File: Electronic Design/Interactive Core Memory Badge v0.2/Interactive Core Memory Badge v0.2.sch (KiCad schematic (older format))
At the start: 59 parts, among them Q1 MMBT4403LT1G, Q10 MMBT4401LT1G, Q11 MMBT4403LT1G, Q12 MMBT4401LT1G, Q13 MMBT4403LT1G, Q14 MMBT4401LT1G, Q15 MMBT4403LT1G, Q16 MMBT4401LT1G, Q17 MMBT4403LT1G, Q18 MMBT4401LT1G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

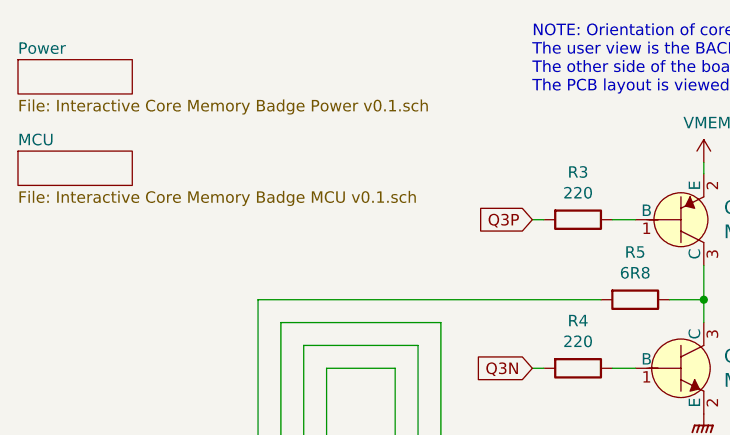
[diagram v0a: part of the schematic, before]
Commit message: Adding discrete OR gate
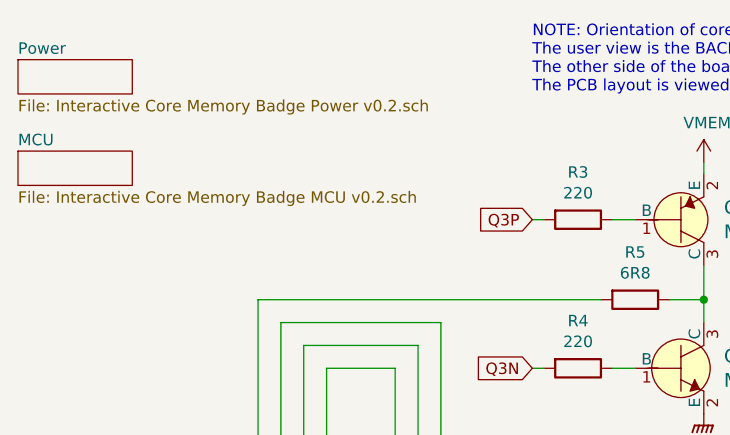
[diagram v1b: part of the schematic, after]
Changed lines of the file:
@@
 EESchema Schematic File Version 4
+LIBS:Interactive Core Memory Badge v0.2-cache
 EELAYER 29 0
 EELAYER END
@@
 U 5D254AE8
 F0 "Power" 50
-F1 "Interactive Core Memory Badge Power v0.1.sch" 50
+F1 "Interactive Core Memory Badge Power v0.2.sch" 50
 $EndSheet
 $Sheet
@@
 U 5D2551FF
 F0 "MCU" 50
-F1 "Interactive Core Memory Badge MCU v0.1.sch" 50
+F1 "Interactive Core Memory Badge MCU v0.2.sch" 50
 $EndSheet
 Text GLabel 1750 4600 3    50   Input ~ 0

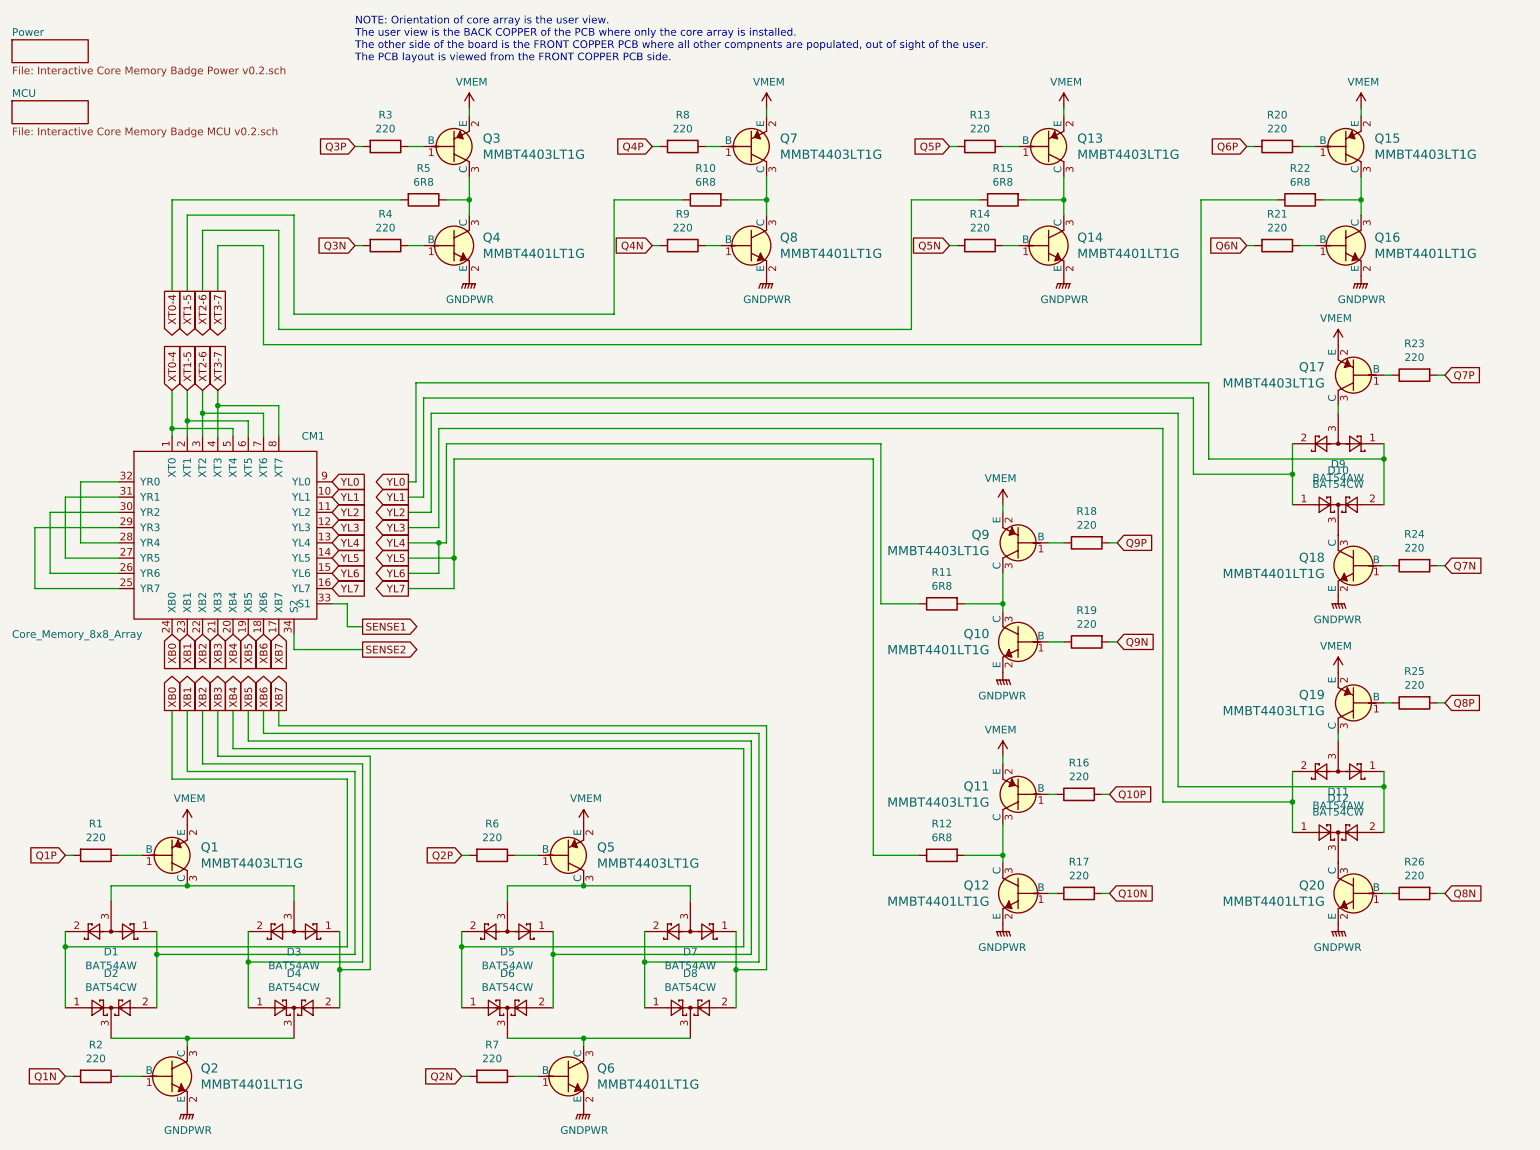
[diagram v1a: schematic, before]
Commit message: Updated drive transistors, switch/diode, OR gate, layout
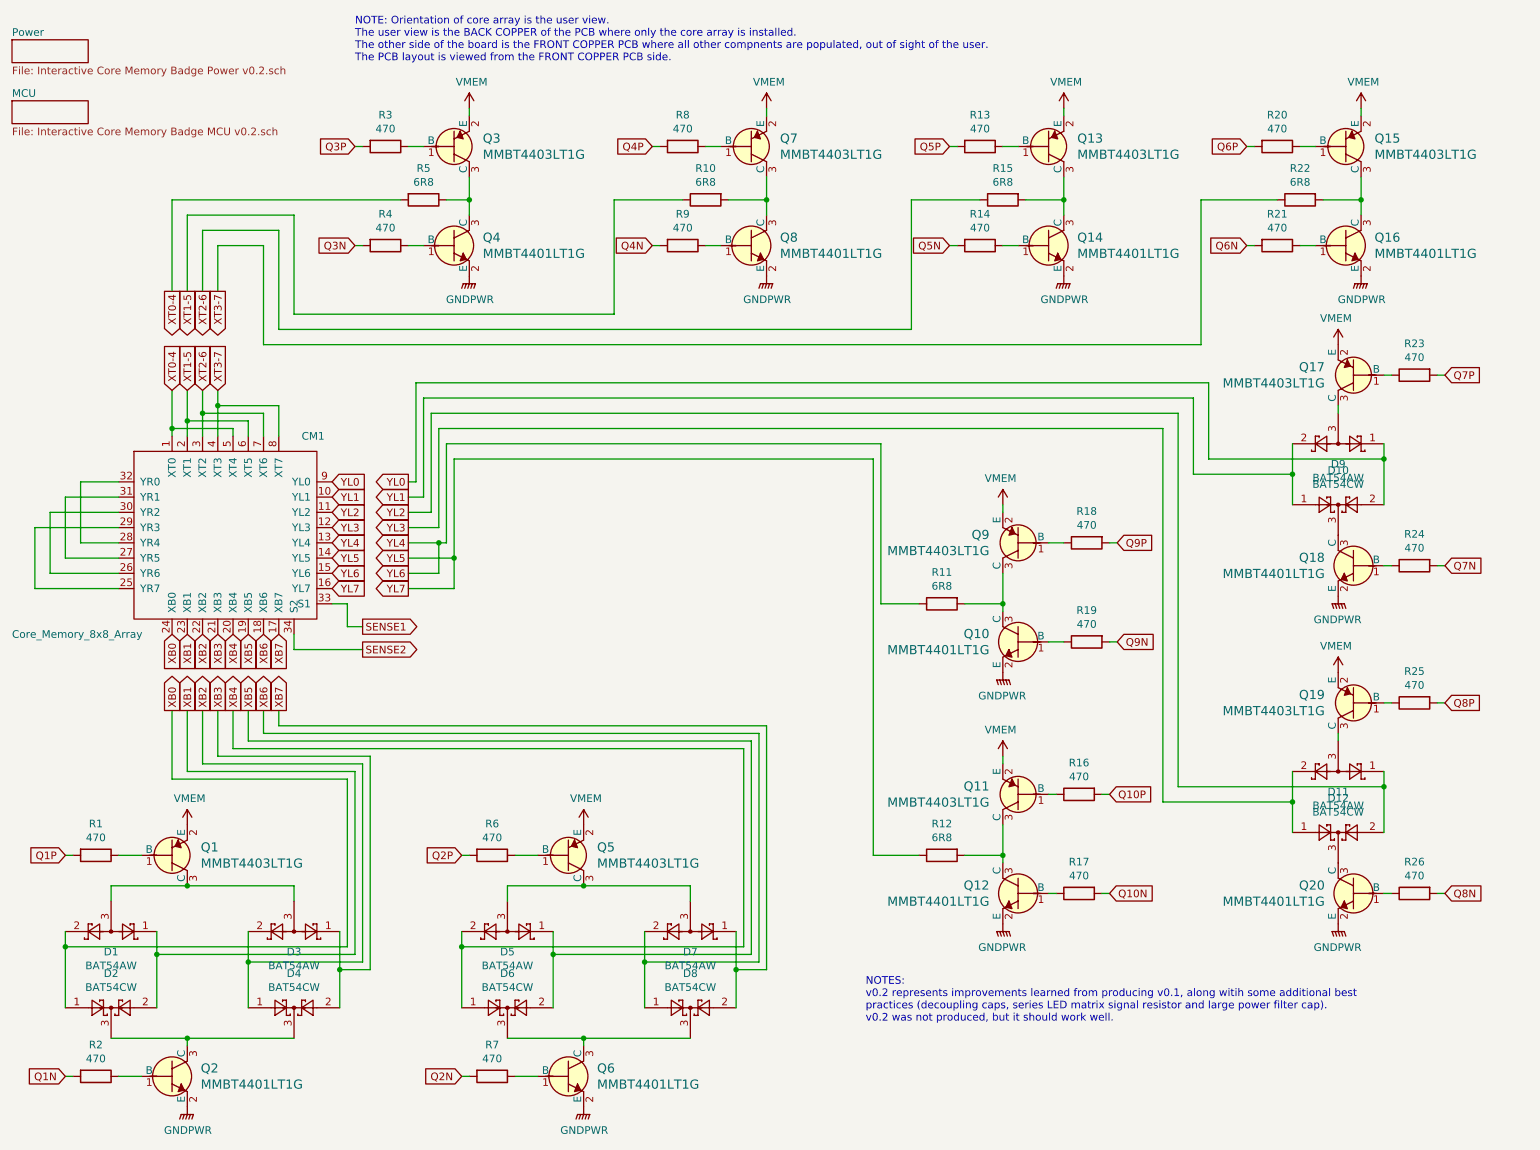
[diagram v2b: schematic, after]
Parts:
- R1, R13, R14, R16, R17, R18, R19, R2, R20, R21, R23, R24, R25, R26, R3, R4, R6, R7, R8, R9: value 220 -> 470
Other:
- note added: "NOTES:\nv0.2 represents improvements learned from producing v0.1, along witih some additional best\npractices (decoupling caps, series LED matrix signal resistor and large power filter cap).\nv0.2 was not produced, but it should work well."
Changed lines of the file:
@@
 encoding utf-8
 Sheet 1 3
-Title "Core 64"
-Date "2019-07-09"
-Rev "0.1"
-Comp "Andy Geppert"
+Title "Core 64 - Interactive Core Memory Badge"
+Date "2020-03-05"
+Rev "0.2"
+Comp "Andy Geppert - Machine Ideas, LLC"
 Comment1 ""
 Comment2 ""
@@
 P 3150 1400
 F 0 "R3" V 2943 1400 50  0000 C CNN
-F 1 "220" V 3034 1400 50  0000 C CNN
+F 1 "470" V 3034 1400 50  0000 C CNN
 F 2 "Resistor_SMD:R_0805_2012Metric" V 3080 1400 50  0001 C CNN
 F 3 "~" H 3150 1400 50  0001 C CNN
@@
 P 3150 2050
 F 0 "R4" V 2943 2050 50  0000 C CNN
-F 1 "220" V 3034 2050 50  0000 C CNN
+F 1 "470" V 3034 2050 50  0000 C CNN
 F 2 "Resistor_SMD:R_0805_2012Metric" V 3080 2050 50  0001 C CNN
 F 3 "~" H 3150 2050 50  0001 C CNN
@@
 P 3850 6050
 F 0 "R6" V 3643 6050 50  0000 C CNN
-F 1 "220" V 3734 6050 50  0000 C CNN
+F 1 "470" V 3734 6050 50  0000 C CNN
 F 2 "Resistor_SMD:R_0805_2012Metric" V 3780 6050 50  0001 C CNN
 F 3 "~" H 3850 6050 50  0001 C CNN
@@
 P 3850 7500
 F 0 "R7" V 3643 7500 50  0000 C CNN
-F 1 "220" V 3734 7500 50  0000 C CNN
+F 1 "470" V 3734 7500 50  0000 C CNN
 F 2 "Resistor_SMD:R_0805_2012Metric" V 3780 7500 50  0001 C CNN
 F 3 "~" H 3850 7500 50  0001 C CNN
@@
 P 5100 1400
 F 0 "R8" V 4893 1400 50  0000 C CNN
-F 1 "220" V 4984 1400 50  0000 C CNN
+F 1 "470" V 4984 1400 50  0000 C CNN
 F 2 "Resistor_SMD:R_0805_2012Metric" V 5030 1400 50  0001 C CNN
 F 3 "~" H 5100 1400 50  0001 C CNN
@@
 P 5100 2050
 F 0 "R9" V 4893 2050 50  0000 C CNN
-F 1 "220" V 4984 2050 50  0000 C CNN
+F 1 "470" V 4984 2050 50  0000 C CNN
 F 2 "Resistor_SMD:R_0805_2012Metric" V 5030 2050 50  0001 C CNN
 F 3 "~" H 5100 2050 50  0001 C CNN
@@
 P 7050 1400
 F 0 "R13" V 6843 1400 50  0000 C CNN
-F 1 "220" V 6934 1400 50  0000 C CNN
+F 1 "470" V 6934 1400 50  0000 C CNN
 F 2 "Resistor_SMD:R_0805_2012Metric" V 6980 1400 50  0001 C CNN
 F 3 "~" H 7050 1400 50  0001 C CNN
@@
 P 7050 2050
 F 0 "R14" V 6843 2050 50  0000 C CNN
-F 1 "220" V 6934 2050 50  0000 C CNN
+F 1 "470" V 6934 2050 50  0000 C CNN
 F 2 "Resistor_SMD:R_0805_2012Metric" V 6980 2050 50  0001 C CNN
 F 3 "~" H 7050 2050 50  0001 C CNN
@@
 P 9000 1400
 F 0 "R20" V 8793 1400 50  0000 C CNN
-F 1 "220" V 8884 1400 50  0000 C CNN
+F 1 "470" V 8884 1400 50  0000 C CNN
 F 2 "Resistor_SMD:R_0805_2012Metric" V 8930 1400 50  0001 C CNN
 F 3 "~" H 9000 1400 50  0001 C CNN
@@
 P 9000 2050
 F 0 "R21" V 8793 2050 50  0000 C CNN
-F 1 "220" V 8884 2050 50  0000 C CNN
+F 1 "470" V 8884 2050 50  0000 C CNN
 F 2 "Resistor_SMD:R_0805_2012Metric" V 8930 2050 50  0001 C CNN
 F 3 "~" H 9000 2050 50  0001 C CNN
@@
 P 9900 2900
 F 0 "R23" V 9693 2900 50  0000 C CNN
-F 1 "220" V 9784 2900 50  0000 C CNN
+F 1 "470" V 9784 2900 50  0000 C CNN
 F 2 "Resistor_SMD:R_0805_2012Metric" V 9830 2900 50  0001 C CNN
 F 3 "~" H 9900 2900 50  0001 C CNN
@@
 P 9900 4150
 F 0 "R24" V 9693 4150 50  0000 C CNN
-F 1 "220" V 9784 4150 50  0000 C CNN
+F 1 "470" V 9784 4150 50  0000 C CNN
 F 2 "Resistor_SMD:R_0805_2012Metric" V 9830 4150 50  0001 C CNN
 F 3 "~" H 9900 4150 50  0001 C CNN
@@
 P 9900 5050
 F 0 "R25" V 9693 5050 50  0000 C CNN
-F 1 "220" V 9784 5050 50  0000 C CNN
+F 1 "470" V 9784 5050 50  0000 C CNN
 F 2 "Resistor_SMD:R_0805_2012Metric" V 9830 5050 50  0001 C CNN
 F 3 "~" H 9900 5050 50  0001 C CNN
@@
 P 9900 6300
 F 0 "R26" V 9693 6300 50  0000 C CNN
-F 1 "220" V 9784 6300 50  0000 C CNN
+F 1 "470" V 9784 6300 50  0000 C CNN
 F 2 "Resistor_SMD:R_0805_2012Metric" V 9830 6300 50  0001 C CNN
 F 3 "~" H 9900 6300 50  0001 C CNN
@@
 P 7750 4000
 F 0 "R18" V 7543 4000 50  0000 C CNN
-F 1 "220" V 7634 4000 50  0000 C CNN
+F 1 "470" V 7634 4000 50  0000 C CNN
 F 2 "Resistor_SMD:R_0805_2012Metric" V 7680 4000 50  0001 C CNN
 F 3 "~" H 7750 4000 50  0001 C CNN
@@
 P 7750 4650
 F 0 "R19" V 7543 4650 50  0000 C CNN
-F 1 "220" V 7634 4650 50  0000 C CNN
+F 1 "470" V 7634 4650 50  0000 C CNN
 F 2 "Resistor_SMD:R_0805_2012Metric" V 7680 4650 50  0001 C CNN
 F 3 "~" H 7750 4650 50  0001 C CNN
@@
 P 7700 5650
 F 0 "R16" V 7493 5650 50  0000 C CNN
-F 1 "220" V 7584 5650 50  0000 C CNN
+F 1 "470" V 7584 5650 50  0000 C CNN
 F 2 "Resistor_SMD:R_0805_2012Metric" V 7630 5650 50  0001 C CNN
 F 3 "~" H 7700 5650 50  0001 C CNN
@@
 P 7700 6300
 F 0 "R17" V 7493 6300 50  0000 C CNN
-F 1 "220" V 7584 6300 50  0000 C CNN
+F 1 "470" V 7584 6300 50  0000 C CNN
 F 2 "Resistor_SMD:R_0805_2012Metric" V 7630 6300 50  0001 C CNN
 F 3 "~" H 7700 6300 50  0001 C CNN
@@
 P 1250 6050
 F 0 "R1" V 1043 6050 50  0000 C CNN
-F 1 "220" V 1134 6050 50  0000 C CNN
+F 1 "470" V 1134 6050 50  0000 C CNN
 F 2 "Resistor_SMD:R_0805_2012Metric" V 1180 6050 50  0001 C CNN
 F 3 "~" H 1250 6050 50  0001 C CNN
@@
 P 1250 7500
 F 0 "R2" V 1043 7500 50  0000 C CNN
-F 1 "220" V 1134 7500 50  0000 C CNN
+F 1 "470" V 1134 7500 50  0000 C CNN
 F 2 "Resistor_SMD:R_0805_2012Metric" V 1180 7500 50  0001 C CNN
 F 3 "~" H 1250 7500 50  0001 C CNN
@@
 	1    0    0    -1
 $EndComp
+Text Notes 6300 7150 0    50   ~ 0
+NOTES:\nv0.2 represents improvements learned from producing v0.1, along witih some additional best\npractices (decoupling caps, series LED matrix signal resistor and large power filter cap).\nv0.2 was not produced, but it should work well.
 $EndSCHEMATC

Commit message: Tweaks to V0.2 schematic and layout from notes.
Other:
- note added: "COL 0"
- note added: "COL 0,4"
- note added: "COL 1"
- note added: "COL 1,5"
- note added: "COL 2"
- note added: "COL 2,6"
- note added: "COL 3"
- note added: "COL 3,7"
- note added: "COL 4"
- note added: "COL 5"
- note added: "COL 6"
- note added: "COL 7"
- note added: "Drive Transistor current: 3.3/470=7mA (too much for Teensy LC)\nMatrix 1/2 select current: 3.3/6.8= 485 mA (does not acccount \nfor voltage drop in transistors)"
- note added: "ROW 0,4"
- note added: "ROW 0,4\nROW 2,6"
- note added: "ROW 1,5"
- note added: "ROW 1,5\nROW 3,7"
- note added: "ROW 2,6"
- note added: "ROW 3,7"
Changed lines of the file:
@@
 Text Notes 6300 7150 0    50   ~ 0
 NOTES:\nv0.2 represents improvements learned from producing v0.1, along witih some additional best\npractices (decoupling caps, series LED matrix signal resistor and large power filter cap).\nv0.2 was not produced, but it should work well.
+Text Notes 3700 3850 0    50   ~ 0
+Drive Transistor current: 3.3/470=7mA (too much for Teensy LC)\nMatrix 1/2 select current: 3.3/6.8= 485 mA (does not acccount \nfor voltage drop in transistors)
+Text Notes 2800 1700 0    50   ~ 0
+COL 0,4
+Text Notes 4650 1700 0    50   ~ 0
+COL 1,5
+Text Notes 6600 1700 0    50   ~ 0
+COL 2,6
+Text Notes 8500 1700 0    50   ~ 0
+COL 3,7
+Text Notes 1700 6600 0    50   ~ 0
+COL 0
+Text Notes 1750 6800 0    50   ~ 0
+COL 1
+Text Notes 2000 6950 0    50   ~ 0
+COL 2
+Text Notes 2900 6950 0    50   ~ 0
+COL 3
+Text Notes 4300 6600 0    50   ~ 0
+COL 4
+Text Notes 4350 6800 0    50   ~ 0
+COL 5
+Text Notes 4600 6900 0    50   ~ 0
+COL 6
+Text Notes 5500 6900 0    50   ~ 0
+COL 7
+Text Notes 6400 4600 0    50   ~ 0
+ROW 0,4\nROW 2,6
+Text Notes 6400 6250 0    50   ~ 0
+ROW 1,5\nROW 3,7
+Text Notes 8700 3400 0    50   ~ 0
+ROW 0,4
+Text Notes 8700 5850 0    50   ~ 0
+ROW 3,7
+Text Notes 8700 3700 0    50   ~ 0
+ROW 1,5
+Text Notes 8700 5550 0    50   ~ 0
+ROW 2,6
 $EndSCHEMATC

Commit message: Update v0.2 with correct Pimoroni footprint
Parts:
- CM1: footprint Core_Memory_8x8_Array:core_64 -> Core_Memory_8x8_Array:core_64_x6.7_y6.5mm
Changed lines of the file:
@@
 F 0 "CM1" H 2600 4600 50  0000 L CNN
 F 1 "Core_Memory_8x8_Array" H 700 3300 50  0000 L CNN
-F 2 "Core_Memory_8x8_Array:core_64" H 2150 4000 50  0001 C CNN
+F 2 "Core_Memory_8x8_Array:core_64_x6.7_y6.5mm" H 2150 4000 50  0001 C CNN
 F 3 "" H 2150 4000 50  0001 C CNN
 	1    2100 3950
